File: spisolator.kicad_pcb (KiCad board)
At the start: 2 copper layers, 16.5 x 22.9 mm, 8 parts, among them P1 CONN_01X06, P2 CONN_02X04, U1 4066, U2 SPI_TGT

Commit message: to be released stuff, r2 of the PCB
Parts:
- D1, R1: moved to B.Cu
- moved R2 12.8 mm to (154.9, 111.1)
- moved R1 4.44 mm to (142.2, 111.1)
- moved D1 4.02 mm to (142.2, 116.8), turned to 270 degrees
- moved U2 1.91 mm to (148.6, 112.4)
- moved C1 1.27 mm to (154.9, 116.2)
- moved P2 1.27 mm to (144.8, 105.4)
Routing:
- net GND: track 67.4 -> 39.5 mm
- net /BUFEN: track 27.7 -> 45.7 mm, vias 2 -> 0
- net +3V3: track 38.8 -> 45.2 mm
- net /MISO: track 26.5 -> 22.6 mm
- net /~MBCS: track 12.1 -> 9.64 mm
- net /MOSI: track 18.8 -> 16.6 mm
- net /MB3V3: track 7.28 -> 8.95 mm
- net /SCK: track 17.3 -> 16.0 mm
- net /~CS: track 16.2 -> 16.9 mm
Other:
- board size 16.5 x 22.9 mm -> 16.5 x 21.6 mm
- board text added: "UR/160129"

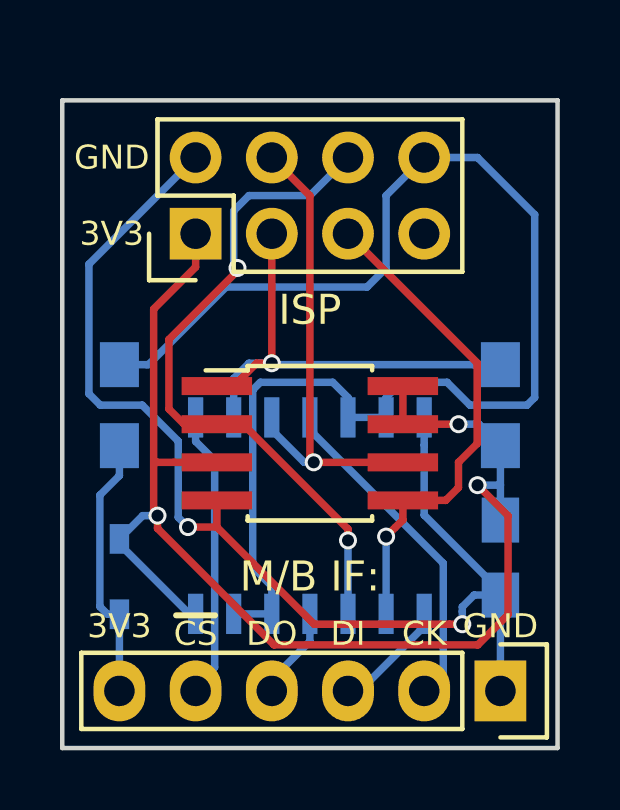
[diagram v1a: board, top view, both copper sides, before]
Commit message: Fix swapped MISO/MOSI in the programming connector
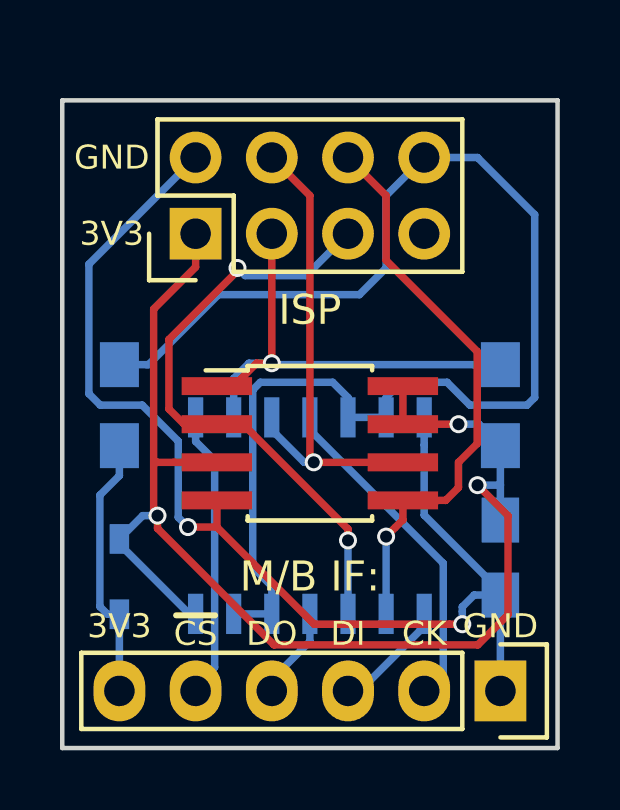
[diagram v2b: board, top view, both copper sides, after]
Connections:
- P2 pad 5: /MOSI -> /MISO
- P2 pad 6: /MISO -> /MOSI
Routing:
- net /MOSI: track 16.6 -> 19.1 mm
- net /MISO: track 22.6 -> 20.5 mm
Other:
- board text added: "UR/170810"
- board text removed: "UR/160129"
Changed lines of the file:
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@@
-(kicad_pcb (version 4) (host pcbnew 4.0.1-stable)
+(kicad_pcb (version 4) (host pcbnew 4.0.6)
   (general
     (links 31)
     (no_connects 0)
-    (area 138.555 100.301666 160.048334 126.725)
+    (area 138.705 100.376666 159.973334 126.825)
     (thickness 1.6)
     (drawings 16)
@@
       (net 9 /SCK))
     (pad 5 thru_hole oval (at 0 5.08 90) (size 1.7272 1.7272) (drill 1.016) (layers *.Cu *.Mask F.SilkS)
+      (net 11 /MISO))
+    (pad 6 thru_hole oval (at 2.54 5.08 90) (size 1.7272 1.7272) (drill 1.016) (layers *.Cu *.Mask F.SilkS)
       (net 10 /MOSI))
-    (pad 6 thru_hole oval (at 2.54 5.08 90) (size 1.7272 1.7272) (drill 1.016) (layers *.Cu *.Mask F.SilkS)
-      (net 11 /MISO))
     (pad 7 thru_hole oval (at 0 7.62 90) (size 1.7272 1.7272) (drill 1.016) (layers *.Cu *.Mask F.SilkS))
     (pad 8 thru_hole oval (at 2.54 7.62 90) (size 1.7272 1.7272) (drill 1.016) (layers *.Cu *.Mask F.SilkS)
@@
     )
   )
-  (gr_text UR/160129 (at 148.59 108.7755) (layer B.SilkS)
+  (gr_text UR/170810 (at 148.59 108.7755) (layer B.SilkS)
     (effects (font (size 0.8 0.8) (thickness 0.2)) (justify mirror))
   )
@@
   (segment (start 151.69 113.03) (end 148.717006 113.03) (width 0.25) (layer F.Cu) (net 9))
   (via (at 148.717006 113.03) (size 0.6) (drill 0.4) (layers F.Cu B.Cu) (net 9))
+  (segment (start 151.69 114.3) (end 153.115 114.3) (width 0.25) (layer F.Cu) (net 10))
+  (segment (start 153.115 114.3) (end 153.543 113.872) (width 0.25) (layer F.Cu) (net 10))
+  (segment (start 153.543 113.872) (end 153.543 113.03) (width 0.25) (layer F.Cu) (net 10))
+  (segment (start 151.13 104.14) (end 149.86 102.87) (width 0.25) (layer F.Cu) (net 10))
+  (segment (start 153.543 113.03) (end 154.168001 112.404999) (width 0.25) (layer F.Cu) (net 10))
+  (segment (start 151.13 106.299) (end 151.13 104.14) (width 0.25) (layer F.Cu) (net 10))
+  (segment (start 154.168001 112.404999) (end 154.168001 109.337001) (width 0.25) (layer F.Cu) (net 10))
+  (segment (start 154.168001 109.337001) (end 151.13 106.299) (width 0.25) (layer F.Cu) (net 10))
   (segment (start 151.429999 115.206501) (end 151.13 115.5065) (width 0.25) (layer F.Cu) (net 10))
   (segment (start 151.69 114.9465) (end 151.429999 115.206501) (width 0.25) (layer F.Cu) (net 10))
@@
   (segment (start 151.13 118.083) (end 151.13 115.5065) (width 0.25) (layer B.Cu) (net 10))
   (via (at 151.13 115.5065) (size 0.6) (drill 0.4) (layers F.Cu B.Cu) (net 10))
-  (segment (start 151.69 114.3) (end 153.115 114.3) (width 0.25) (layer F.Cu) (net 10))
-  (segment (start 153.115 114.3) (end 153.543 113.872) (width 0.25) (layer F.Cu) (net 10))
-  (segment (start 153.543 113.872) (end 153.543 113.03) (width 0.25) (layer F.Cu) (net 10))
-  (segment (start 153.543 113.03) (end 154.168001 112.404999) (width 0.25) (layer F.Cu) (net 10))
-  (segment (start 154.168001 109.718001) (end 149.86 105.41) (width 0.25) (layer F.Cu) (net 10))
-  (segment (start 154.168001 112.404999) (end 154.168001 109.718001) (width 0.25) (layer F.Cu) (net 10))
+  (segment (start 149.86 105.41) (end 148.463 106.807) (width 0.25) (layer B.Cu) (net 11))
+  (segment (start 148.463 106.807) (end 146.431 106.807) (width 0.25) (layer B.Cu) (net 11))
+  (segment (start 146.431 106.807) (end 146.177 106.553) (width 0.25) (layer B.Cu) (net 11))
   (segment (start 146.177 106.553) (end 146.177 106.649087) (width 0.25) (layer F.Cu) (net 11))
   (segment (start 146.177 106.649087) (end 143.891 108.935087) (width 0.25) (layer F.Cu) (net 11))
@@
   (segment (start 143.891 111.252) (end 144.399 111.76) (width 0.25) (layer F.Cu) (net 11))
   (segment (start 144.399 111.76) (end 145.49 111.76) (width 0.25) (layer F.Cu) (net 11))
-  (segment (start 146.177 106.553) (end 146.05 106.426) (width 0.25) (layer B.Cu) (net 11))
-  (segment (start 146.05 106.426) (end 146.05 104.648) (width 0.25) (layer B.Cu) (net 11))
-  (segment (start 146.05 104.648) (end 146.558 104.14) (width 0.25) (layer B.Cu) (net 11))
-  (segment (start 146.558 104.14) (end 148.59 104.14) (width 0.25) (layer B.Cu) (net 11))
-  (segment (start 148.59 104.14) (end 149.86 102.87) (width 0.25) (layer B.Cu) (net 11))
   (via (at 146.177 106.553) (size 0.6) (drill 0.4) (layers F.Cu B.Cu) (net 11))
   (segment (start 149.86 115.255) (end 149.86 115.6335) (width 0.25) (layer F.Cu) (net 11))
@@
   (segment (start 149.86 118.083) (end 149.86 115.6335) (width 0.25) (layer B.Cu) (net 11))
   (via (at 149.86 115.6335) (size 0.6) (drill 0.4) (layers F.Cu B.Cu) (net 11))
+  (segment (start 152.4 102.87) (end 151.13 104.14) (width 0.25) (layer B.Cu) (net 12))
+  (segment (start 151.13 104.14) (end 151.13 106.553) (width 0.25) (layer B.Cu) (net 12))
+  (segment (start 143.209 109.775) (end 143.14 109.775) (width 0.25) (layer B.Cu) (net 12))
+  (segment (start 143.14 109.775) (end 142.24 109.775) (width 0.25) (layer B.Cu) (net 12))
+  (segment (start 151.13 106.553) (end 150.241 107.442) (width 0.25) (layer B.Cu) (net 12))
+  (segment (start 150.241 107.442) (end 145.542 107.442) (width 0.25) (layer B.Cu) (net 12))
+  (segment (start 145.542 107.442) (end 143.209 109.775) (width 0.25) (layer B.Cu) (net 12))
   (segment (start 151.13 111.533) (end 151.13 110.871) (width 0.25) (layer B.Cu) (net 12))
   (segment (start 151.13 110.871) (end 151.638 110.363) (width 0.25) (layer B.Cu) (net 12))
@@
   (segment (start 149.352 110.363) (end 149.86 110.871) (width 0.25) (layer B.Cu) (net 12))
   (segment (start 149.86 110.871) (end 149.86 111.533) (width 0.25) (layer B.Cu) (net 12))
-  (segment (start 152.4 102.87) (end 151.13 104.14) (width 0.25) (layer B.Cu) (net 12))
-  (segment (start 151.13 104.14) (end 151.13 106.553) (width 0.25) (layer B.Cu) (net 12))
-  (segment (start 151.13 106.553) (end 150.495 107.188) (width 0.25) (layer B.Cu) (net 12))
-  (segment (start 150.495 107.188) (end 145.796 107.188) (width 0.25) (layer B.Cu) (net 12))
-  (segment (start 145.796 107.188) (end 143.209 109.775) (width 0.25) (layer B.Cu) (net 12))
-  (segment (start 143.209 109.775) (end 143.14 109.775) (width 0.25) (layer B.Cu) (net 12))
-  (segment (start 143.14 109.775) (end 142.24 109.775) (width 0.25) (layer B.Cu) (net 12))
   (segment (start 149.86 111.533) (end 151.13 111.533) (width 0.25) (layer B.Cu) (net 12))
   (segment (start 147.32 118.083) (end 146.05 118.083) (width 0.25) (layer B.Cu) (net 12))
